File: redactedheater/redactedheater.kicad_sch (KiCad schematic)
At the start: 36 parts, among them Q1 NMOS DIT150N03-DIN, Q2 NPN BC-174B-CDI, Q3 NPN BC-174B-CDI, U1 L7805, U2 MLX90614ESF-BAA-000-TU, U3 MCP6002-xP

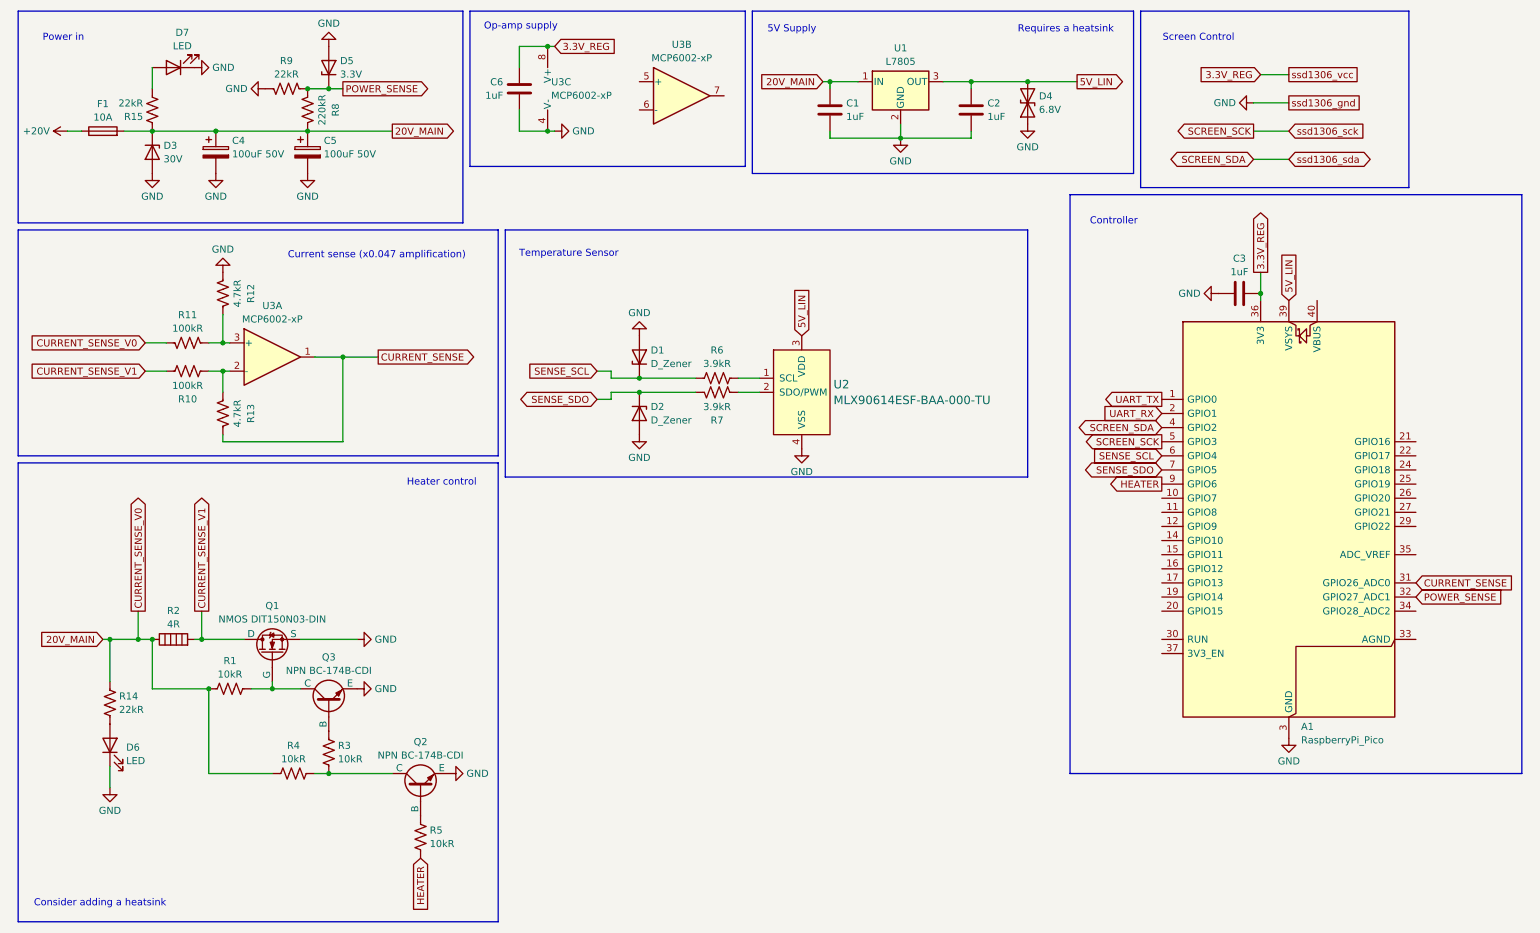
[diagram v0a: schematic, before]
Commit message: working pwm
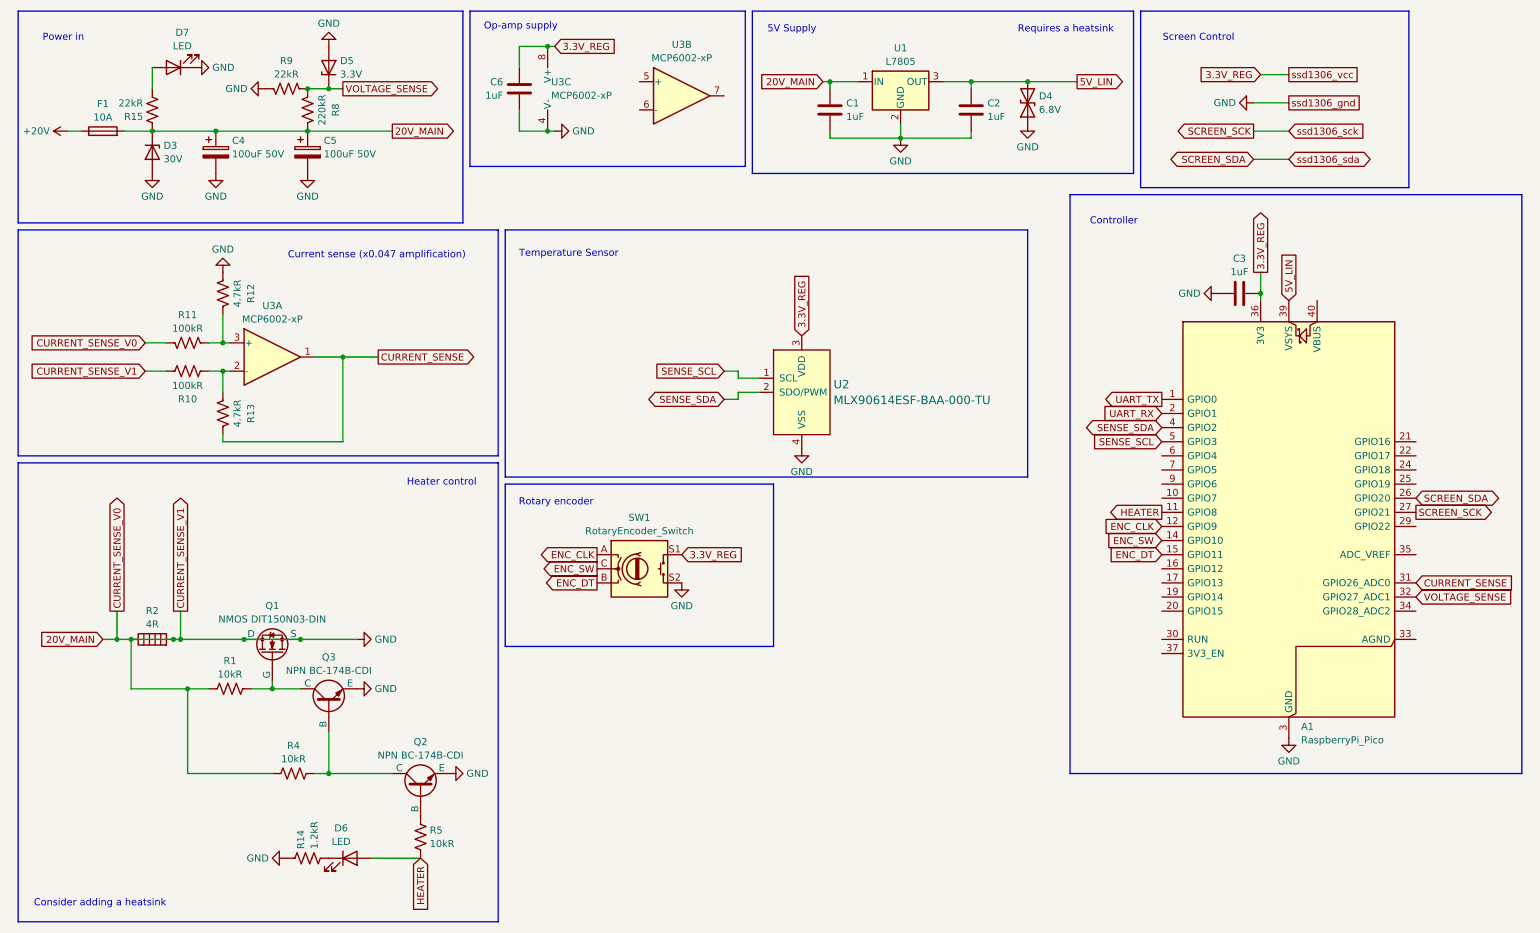
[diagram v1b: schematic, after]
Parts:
- removed D1, D2: D_Zener, symbol Device:D_Zener
- removed R3: 10kR, symbol Device:R_US
- removed R6, R7: 3.9kR, symbol Device:R_US
- added SW1: RotaryEncoder_Switch, symbol Device:RotaryEncoder_Switch
- R14: value 22kR -> 1.2kR
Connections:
- net 20V_MAIN is gone; now on net GND: C1.1, C4.1, C5.1, D3.1 (K), F1.2, R1.1, R11.2, R14.2, R15.2, R2.1, R4.1, R8.1, U1.1 (IN)
- net CURRENT_SENSE_V1 is gone; now on net GND: Q1.1 (D), R10.2, R2.2
- net 3.3V_REG: now also U2.3 (VDD), SW1.S1
- net 5V_LIN: no longer U2.3 (VDD)
- net GND: now also SW1.S2; no longer D6.1 (K)
- net HEATER: now also A1.11 (GPIO8), D6.2 (A); no longer A1.9 (GPIO6)
- net SCREEN_SCK: now also A1.27 (GPIO21); no longer A1.5 (GPIO3)
- net SCREEN_SDA: now also A1.26 (GPIO20); no longer A1.4 (GPIO2)
- net SENSE_SCL: now also A1.5 (GPIO3), U2.1 (SCL); no longer A1.6 (GPIO4)
- net at Q2.1 (C), R4.2: now also Q3.2 (B)
- net at R14.1: now also D6.1 (K); no longer D6.2 (A)
- net SENSE_SDA: now reaches U2.2 (SDO/PWM)
- net SENSE_SDA: now also A1.4 (GPIO2)
- net ENC_CLK: now reaches A1.12 (GPIO9)
- net ENC_CLK: now also SW1.A
- net ENC_SW: now reaches A1.14 (GPIO10)
- net ENC_SW: now also SW1.C
- net ENC_DT: now reaches A1.15 (GPIO11)
- net ENC_DT: now also SW1.B
- net POWER_SENSE renamed VOLTAGE_SENSE
- net SENSE_SDO: no longer names the net of A1.7 (GPIO5)
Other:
- note added: "Rotary encoder"
- moved on the sheet: D6, R14, R2
